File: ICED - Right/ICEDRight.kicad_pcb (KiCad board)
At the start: 2 copper layers, 175.4 x 145 mm, 163 parts, among them P1 FLASH_HDR, P2 USBC, P3 CONN_17, P4 USB3_AFEMALE, P5 RGB Out, Q1 TC1264, U1 MK20DX256VLH7, U2 IS31FL3737-QFLS4-TR, X1 CRYSTAL

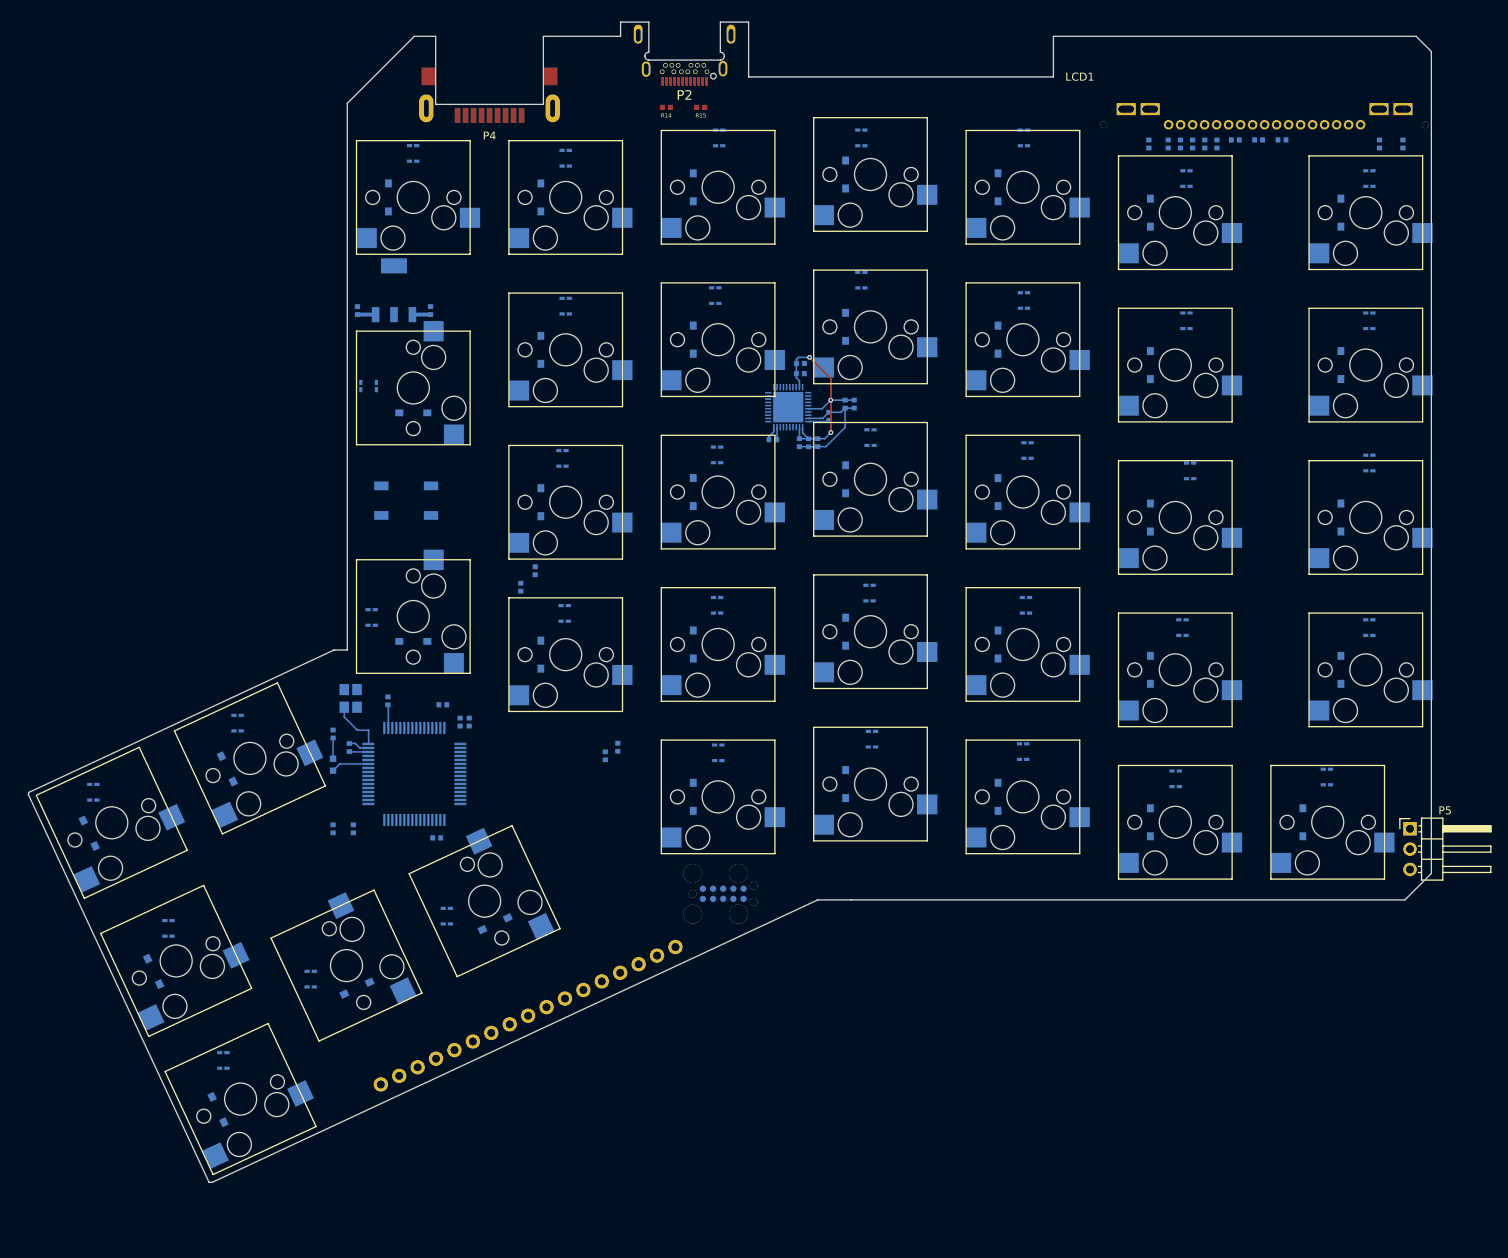
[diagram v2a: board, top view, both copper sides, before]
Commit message: LED orientation and start routing around main mcu
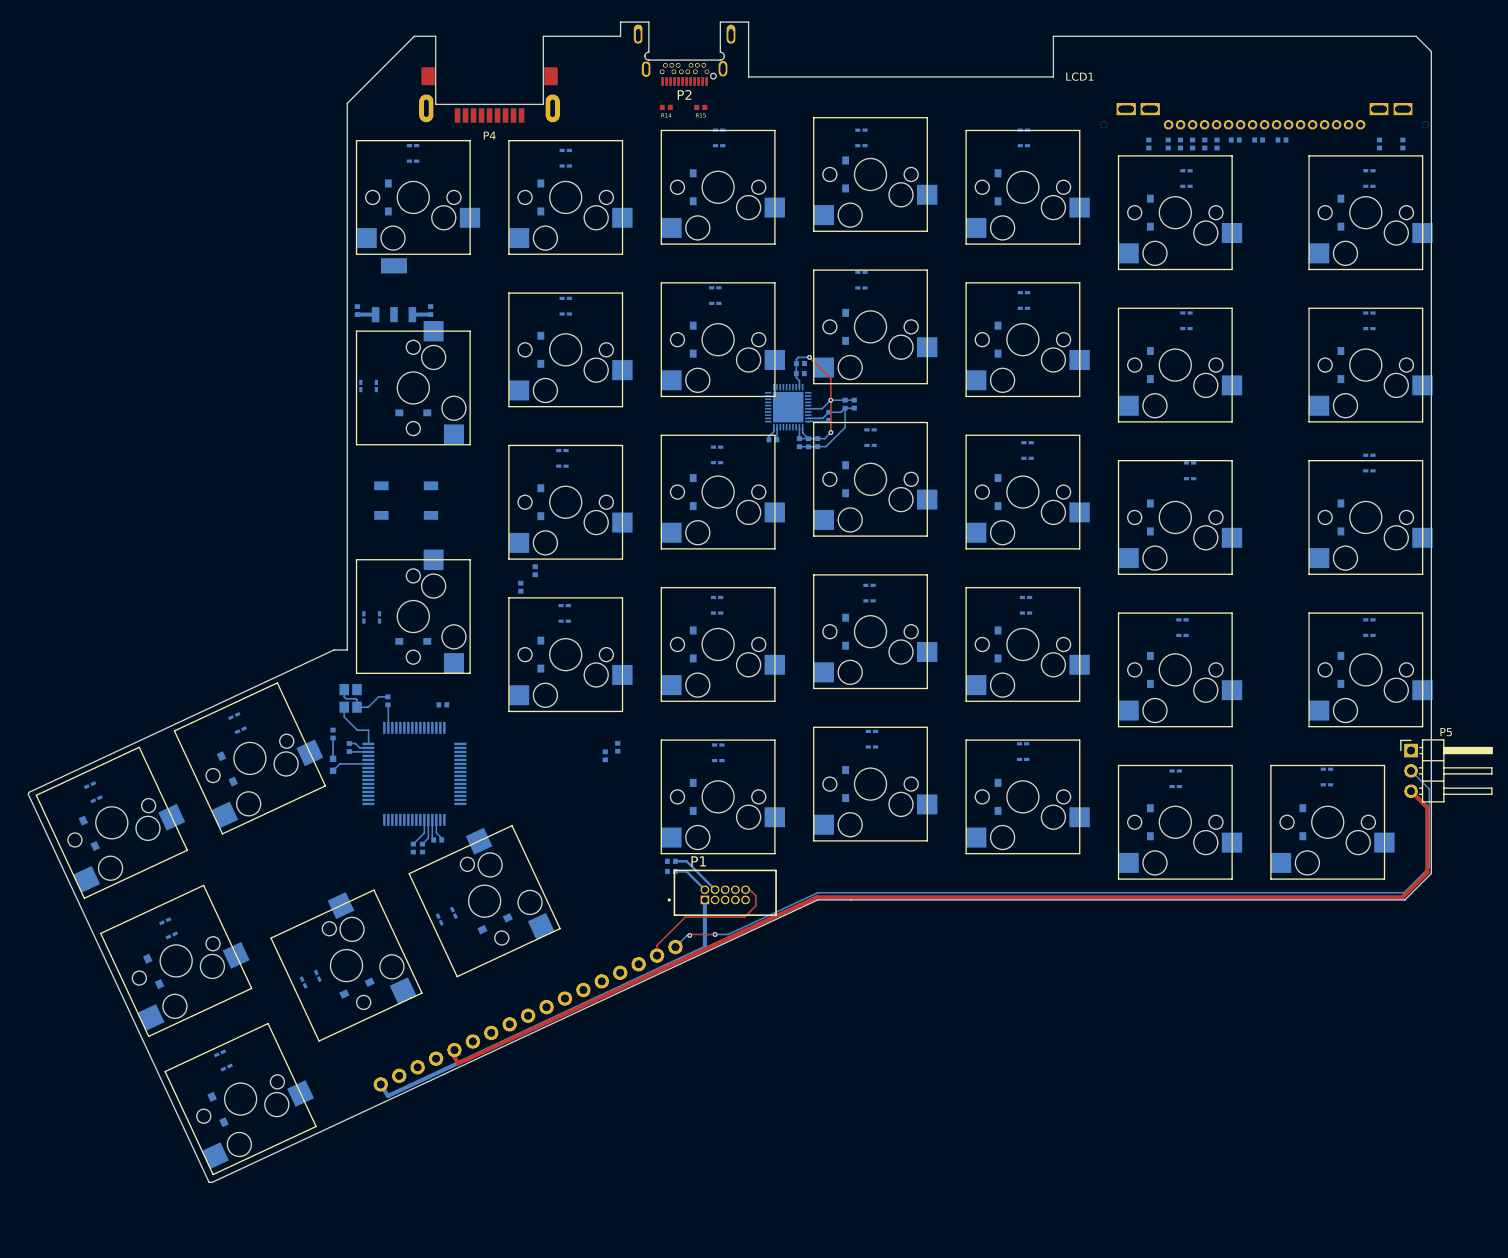
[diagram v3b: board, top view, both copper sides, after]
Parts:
- P1: value FLASH_HDR -> Conn_ARM_JTAG_SWD_10; footprint prettylib:JLINK_NEEDLE -> prettylib:SHF-105-01-L-D-TH; moved to F.Cu
- moved R7 42.6 mm to (104.6, 149.4), turned to -90 degrees
- moved R6 40.0 mm to (104.6, 148.1), turned to -90 degrees
- moved R1 16.8 mm to (73.5, 146.4), turned to 0 degrees
- moved R2 16.8 mm to (72.4, 146.4), turned to 0 degrees
- moved P5 9.78 mm to (197.1, 134.2)
- moved P1 0.28 mm to (111.4, 152.3)
- moved C4 0.28 mm to (75.4, 145.4)
- turned LED21 to -155 degrees
- turned LED22 to -155 degrees
- turned LED23 to -90 degrees
- turned LED30 to -155 degrees
- turned LED31 to -155 degrees
- turned LED32 to -65 degrees
- turned LED33 to -65 degrees
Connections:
- P1 pad 5: +5V -> VSS
- P1 pad 7: /mcu/TX2 -> unconnected-(P1-Pad7)
- P1 pad 9: /mcu/PTA5 -> VSS
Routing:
- net +5V: track 2.28 -> 142.1 mm
- net /mcu/RGBOUT: track 0.00 -> 110.4 mm, vias 0 -> 2
- net VDD: track 33.9 -> 88.6 mm
- net /mcu/MCU_RESET: track 2.91 -> 21.4 mm
- net VSS: track 19.8 -> 30.4 mm
- net /mcu/SWD_CLK: track 0.00 -> 6.43 mm
- net /mcu/SWD_DIO: track 0.00 -> 4.64 mm
- net Net-(R2-Pad2): track 0.00 -> 3.59 mm
- net Net-(R1-Pad2): track 0.00 -> 3.33 mm
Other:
- board text added: "RGBOUT"
- board text removed: "AUD"

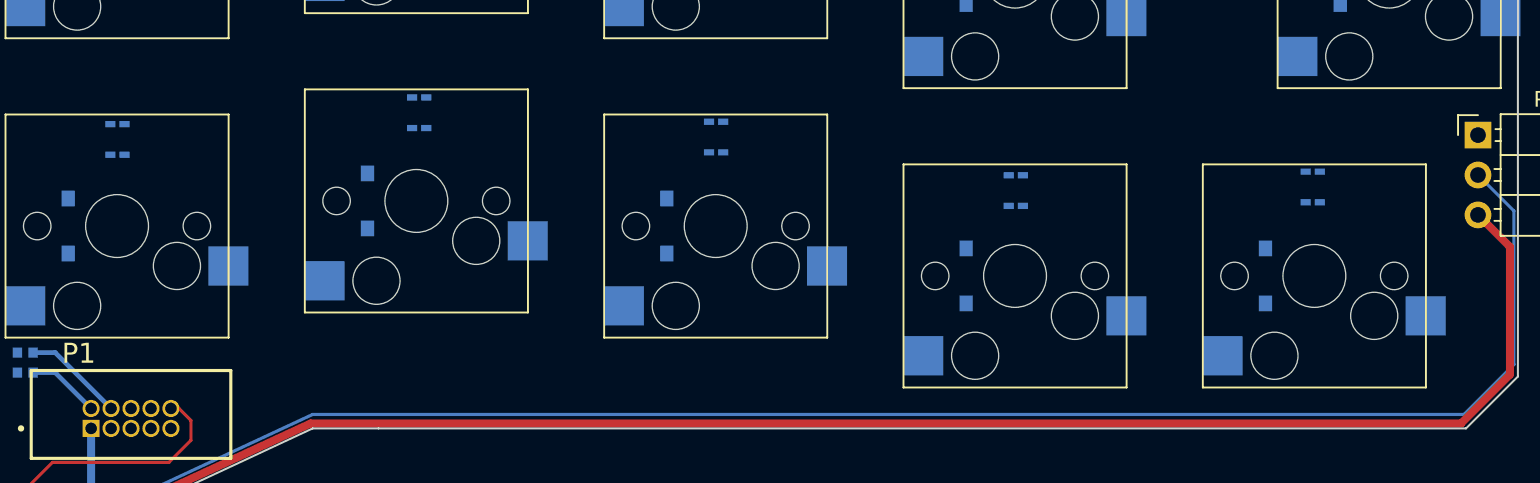
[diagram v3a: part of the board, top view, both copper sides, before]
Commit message: Left: Revert to SMD diodes
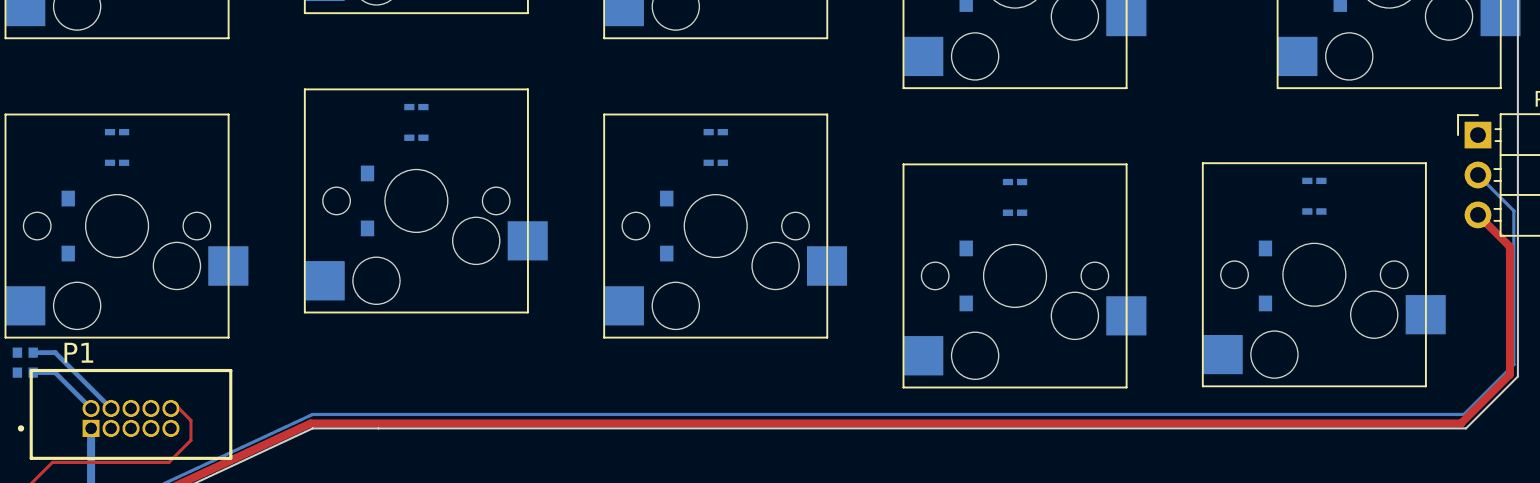
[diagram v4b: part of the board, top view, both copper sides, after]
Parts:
- moved LED36 0.66 mm to (148.6, 135.0)
- moved LED35 0.64 mm to (129.5, 133.4)
- moved LED38 0.60 mm to (186.7, 138.1)
- moved LED34 0.51 mm to (110.5, 135.0)
- moved LED37 0.44 mm to (167.6, 138.2)
- moved S38 0.07 mm to (186.7, 143.1)
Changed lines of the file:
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@@
-(kicad_pcb (version 20210824) (generator pcbnew)
+(kicad_pcb (version 20210925) (generator pcbnew)
   (general
     (thickness 1.6)
@@
   (net 153 "unconnected-(P1-Pad7)")
   (footprint "prettylib:SW_Hotswap_Kailh" (layer "F.Cu")
-    (at 186.69 143.203 180)
+    (at 186.69 143.129 180)
     (descr "Kailh keyswitch Hotswap Socket, ")
     (tags "Kailh Keyboard Keyswitch Switch Hotswap Socket")
@@
   )
   (footprint "prettylib:0606" (layer "B.Cu")
-    (at 129.7178 132.8166)
+    (at 129.54 133.43)
     (property "Sheetfile" "ledmatrix.kicad_sch")
     (property "Sheetname" "ledmatrix_2")
@@
   )
   (footprint "prettylib:0606" (layer "B.Cu")
-    (at 110.5154 134.5184)
+    (at 110.49 135.028)
     (property "Sheetfile" "ledmatrix.kicad_sch")
     (property "Sheetname" "ledmatrix_2")
@@
   )
   (footprint "prettylib:0606" (layer "B.Cu")
-    (at 167.6908 137.7696)
+    (at 167.64 138.203)
     (property "Sheetfile" "ledmatrix.kicad_sch")
     (property "Sheetname" "ledmatrix_2")
@@
     (pad "" np_thru_hole oval locked (at 0 0) (size 2.9 1.25) (drill oval 2.9 1.25) (layers *.Cu *.Mask))
     (pad "1" smd rect locked (at 0.45 0.975) (size 0.65 0.4) (layers "B.Cu" "B.Paste" "B.Mask")
-      (net 148 "/mcu/ledmatrix_2/Row5A") (pinfunction "A") (pintype "passive"))
+      (net 148 "/mcu/ledmatrix_2/Row5A") (pinfunction "A"))
     (pad "2" smd rect locked (at -0.45 0.975) (size 0.65 0.4) (layers "B.Cu" "B.Paste" "B.Mask")
-      (net 130 "/mcu/ledmatrix_2/Red2") (pinfunction "RK") (pintype "passive"))
+      (net 130 "/mcu/ledmatrix_2/Red2") (pinfunction "RK"))
     (pad "3" smd rect locked (at -0.45 -0.975) (size 0.65 0.4) (layers "B.Cu" "B.Paste" "B.Mask")
-      (net 131 "/mcu/ledmatrix_2/Green2") (pinfunction "GK") (pintype "passive"))
+      (net 131 "/mcu/ledmatrix_2/Green2") (pinfunction "GK"))
     (pad "4" smd rect locked (at 0.44958 -0.975) (size 0.65 0.4) (layers "B.Cu" "B.Paste" "B.Mask")
-      (net 132 "/mcu/ledmatrix_2/Blue2") (pinfunction "BK") (pintype "passive"))
+      (net 132 "/mcu/ledmatrix_2/Blue2") (pinfunction "BK"))
     (model "/home/ellie/.local/share/kicad/LTST-C195KGJSKT.STEP"
       (offset (xyz 0 0 0.15))
@@
   )
   (footprint "prettylib:0606" (layer "B.Cu")
-    (at 148.6154 134.366)
+    (at 148.59 135.028)
     (property "Sheetfile" "ledmatrix.kicad_sch")
     (property "Sheetname" "ledmatrix_2")
@@
     (pad "" np_thru_hole oval locked (at 0 0 295) (size 2.9 1.25) (drill oval 2.9 1.25) (layers *.Cu *.Mask))
     (pad "1" smd rect locked (at 0.45 0.975 295) (size 0.65 0.4) (layers "B.Cu" "B.Paste" "B.Mask")
-      (net 147 "/mcu/ledmatrix_2/Row5B") (pinfunction "A") (pintype "passive"))
+      (net 147 "/mcu/ledmatrix_2/Row5B") (pinfunction "A"))
     (pad "2" smd rect locked (at -0.45 0.975 295) (size 0.65 0.4) (layers "B.Cu" "B.Paste" "B.Mask")
-      (net 133 "/mcu/ledmatrix_2/Red1") (pinfunction "RK") (pintype "passive"))
+      (net 133 "/mcu/ledmatrix_2/Red1") (pinfunction "RK"))
     (pad "3" smd rect locked (at -0.45 -0.975 295) (size 0.65 0.4) (layers "B.Cu" "B.Paste" "B.Mask")
-      (net 134 "/mcu/ledmatrix_2/Green1") (pinfunction "GK") (pintype "passive"))
+      (net 134 "/mcu/ledmatrix_2/Green1") (pinfunction "GK"))
     (pad "4" smd rect locked (at 0.44958 -0.975 295) (size 0.65 0.4) (layers "B.Cu" "B.Paste" "B.Mask")
-      (net 135 "/mcu/ledmatrix_2/Blue1") (pinfunction "BK") (pintype "passive"))
+      (net 135 "/mcu/ledmatrix_2/Blue1") (pinfunction "BK"))
     (model "/home/ellie/.local/share/kicad/LTST-C195KGJSKT.STEP"
       (offset (xyz 0 0 0.15))
@@
   )
   (footprint "prettylib:0606" (layer "B.Cu")
-    (at 186.5884 137.541)
+    (at 186.69 138.129)
     (property "Sheetfile" "ledmatrix.kicad_sch")
     (property "Sheetname" "ledmatrix_2")
@@
     (pad "" np_thru_hole oval locked (at 0 0) (size 2.9 1.25) (drill oval 2.9 1.25) (layers *.Cu *.Mask))
     (pad "1" smd rect locked (at 0.45 0.975) (size 0.65 0.4) (layers "B.Cu" "B.Paste" "B.Mask")
-      (net 148 "/mcu/ledmatrix_2/Row5A") (pinfunction "A") (pintype "passive"))
+      (net 148 "/mcu/ledmatrix_2/Row5A") (pinfunction "A"))
     (pad "2" smd rect locked (at -0.45 0.975) (size 0.65 0.4) (layers "B.Cu" "B.Paste" "B.Mask")
-      (net 133 "/mcu/ledmatrix_2/Red1") (pinfunction "RK") (pintype "passive"))
+      (net 133 "/mcu/ledmatrix_2/Red1") (pinfunction "RK"))
     (pad "3" smd rect locked (at -0.45 -0.975) (size 0.65 0.4) (layers "B.Cu" "B.Paste" "B.Mask")
-      (net 134 "/mcu/ledmatrix_2/Green1") (pinfunction "GK") (pintype "passive"))
+      (net 134 "/mcu/ledmatrix_2/Green1") (pinfunction "GK"))
     (pad "4" smd rect locked (at 0.44958 -0.975) (size 0.65 0.4) (layers "B.Cu" "B.Paste" "B.Mask")
-      (net 135 "/mcu/ledmatrix_2/Blue1") (pinfunction "BK") (pintype "passive"))
+      (net 135 "/mcu/ledmatrix_2/Blue1") (pinfunction "BK"))
     (model "/home/ellie/.local/share/kicad/LTST-C195KGJSKT.STEP"
       (offset (xyz 0 0 0.15))

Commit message: More routing
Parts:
- moved R7 42.6 mm to (63.8, 137.4), turned to 180 degrees
- moved R3 41.3 mm to (118.0, 99.7), turned to 90 degrees
- moved R6 40.7 mm to (65.0, 138.9), turned to 180 degrees
- moved R5 40.3 mm to (117.3, 98.6), turned to 90 degrees
- moved R16 35.2 mm to (116.6, 96.6)
- moved R4 32.8 mm to (115.5, 94.5), turned to 180 degrees
- moved C3 2.97 mm to (77.6, 131.1), turned to 0 degrees
- moved X1 2.09 mm to (65.8, 129.4)
- moved LED19 2.02 mm to (167.6, 100.1)
- moved LED20 1.86 mm to (191.5, 100.1)
- moved R14 1.62 mm to (105.2, 52.7), turned to 0 degrees
- moved LED6 1.58 mm to (167.6, 62.0)
- moved C18 1.57 mm to (121.2, 84.3), turned to -90 degrees
- moved C6 1.57 mm to (121.2, 85.6), turned to -90 degrees
- moved LED13 1.50 mm to (167.6, 81.1)
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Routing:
- net /mcu/ledmatrix_2/Red1: track 0.00 -> 410.4 mm, vias 0 -> 16
- net /mcu/ledmatrix_2/Blue1: track 0.00 -> 407.5 mm, vias 0 -> 16
- net /mcu/ledmatrix_2/Green1: track 0.00 -> 401.9 mm, vias 0 -> 16
- net /mcu/ledmatrix_2/Blue3: track 0.00 -> 394.4 mm, vias 0 -> 15
- net /mcu/ledmatrix_2/Green3: track 0.00 -> 393.2 mm, vias 0 -> 16
- net /mcu/ledmatrix_2/Red3: track 0.00 -> 389.7 mm, vias 0 -> 17
- net /mcu/ledmatrix_2/Blue2: track 0.00 -> 381.1 mm, vias 0 -> 14
- net /mcu/ledmatrix_2/Red2: track 0.00 -> 380.2 mm, vias 0 -> 14
- net /mcu/ledmatrix_2/Green2: track 0.00 -> 374.1 mm, vias 0 -> 14
- net /Row5: track 0.00 -> 206.9 mm, vias 0 -> 7
- net /mcu/LCD_KR: track 0.00 -> 205.0 mm, vias 0 -> 2
- net /Row1: track 0.00 -> 201.6 mm, vias 0 -> 2
- net /Row4: track 0.00 -> 198.3 mm, vias 0 -> 5
- net /Col9: track 0.00 -> 198.3 mm, vias 0 -> 6
- net /mcu/LCD_KB: track 0.00 -> 195.0 mm, vias 0 -> 2
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- added copper zone on B.Cu, net VSS
